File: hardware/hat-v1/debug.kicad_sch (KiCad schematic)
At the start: 45 parts, among them J5 Tag-Connect TC2050

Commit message: HAT v1 schematic: apply adversarial review (power + digital/security/DFM)
AUTO-ON above buck EN window, BENCH no longer blocks power-off, OVP moved
to 19.2 V with input damper, Tier A parts DNP for JLC, debug links
removable for production, antenna short limited, stock footprints where
available, cap ratings/DC-bias fixes, CONSOLE_TX/RX naming.

Co-Authored-By: Claude Opus 5.5 <noreply@anthropic.com>
Claude-Session: https://claude.ai/code/session_01MLRuxTEmuMV82xcNLE62jW
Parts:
- added R40, R41, R42, R43, R44, R45, R46, R47: 0R, Resistor_SMD:R_0402_1005Metric, symbol batman:R
- added R48: 1k, Resistor_SMD:R_0402_1005Metric, symbol batman:R
- J5: Note UART0 = passwordless root console until #137 ships: release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 -> console = passwordless root until #137 ships: release gate; now left out of the parts list
- TP16, TP17, TP18, TP19, TP20, TP21, TP22, TP23, TP24, TP25, TP26, TP27, TP28, TP29, TP30, TP31, TP32, TP33, TP34, TP35, TP36, TP37, TP38, TP39, TP40, TP41, TP42, TP43, TP44: now left out of the parts list
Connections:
- net 3V3_PI: now also R48.1; no longer J5.1
- net HALOW_BUSY: now also R47.1; no longer J5.10
- net HALOW_IRQ: now also R46.1; no longer J5.9
- net SPI0_CE0: now also R45.1; no longer J5.8
- net SPI0_MISO: now also R44.1; no longer J5.7
- net SPI0_MOSI: now also R43.1; no longer J5.6
- net SPI0_SCLK: now also R42.1; no longer J5.5
- net UART0_RX renamed TC_RX
- net TC_RX: now also R41.2
- net UART0_TX renamed TC_TX
- net TC_TX: now also R40.2
- new net CONSOLE_RX: R41.1
- new net CONSOLE_TX: R40.1
- new net TC_3V3: J5.1, R48.2
- new net TC_BUSY: J5.10, R47.2
- new net TC_CS: J5.8, R45.2
- new net TC_IRQ: J5.9, R46.2
- new net TC_MISO: J5.7, R44.2
- new net TC_MOSI: J5.6, R43.2
- new net TC_SCLK: J5.5, R42.2
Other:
- note added: "NOTES J5: console = passwordless root until #137 ships: release gate R48: sense only: an adapter that drives VCC cannot back-feed the Pi R40: R40-R47 debug links: fitted on dev boards, NOT fitted on production (HaLow keys cross SPI0) TP41: Kelvin pad on the shunt: mV x 100 = mA (R9) TP42: Kelvin pad on the shunt: mV x 100 = mA (R9) TP43: Kelvin pad on the shunt: mV x 100 = mA (R9) TP44: Kelvin pa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"
- note removed: "NOTES J5: UART0 = passwordless root console until #137 ships: release gate TP41: Kelvin pad on the shunt: mV x 100 = mA (R9) TP42: Kelvin pad on the shunt: mV x 100 = mA (R9) TP43: Kelvin pad on the shunt: mV x 100 = mA (R9) TP44: Kelvin pad on the shunt: mV x 100 = mA (R9)"
- moved on the sheet: J5, TP1, TP10, TP11, TP12, TP13, TP14, TP15, TP16, TP17, TP18, TP19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

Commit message: HAT v1: reduce test points (clip pads only for VBAT/5V/3V3 HaLow/GND), re-place
Signals on the 40-pin header are probed on its solder joints; checker
verifies that list. Floorplan: all functional parts and the 4 clip pads
fit; 23 small probe pads still need a home.

Co-Authored-By: Claude Opus 5.5 <noreply@anthropic.com>
Claude-Session: https://claude.ai/code/session_01MLRuxTEmuMV82xcNLE62jW
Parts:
- removed TP30: EN_5V, TestPoint:TestPoint_Pad_D1.0mm, symbol batman:TP
- removed TP31: EN_3V3, TestPoint:TestPoint_Pad_D1.0mm, symbol batman:TP
- removed TP32: PG_5V, TestPoint:TestPoint_Pad_D1.0mm, symbol batman:TP
- removed TP33: BAT_PRESENT_N, TestPoint:TestPoint_Pad_D1.0mm, symbol batman:TP
- removed TP34: EF_FLT_N, TestPoint:TestPoint_Pad_D1.0mm, symbol batman:TP
- removed TP35: EF_SHDN, TestPoint:TestPoint_Pad_D1.0mm, symbol batman:TP
- removed TP36: INA_ALERT_N, TestPoint:TestPoint_Pad_D1.0mm, symbol batman:TP
- removed TP37: RTC_CLKOUT, TestPoint:TestPoint_Pad_D1.0mm, symbol batman:TP
- removed TP38: RTC_INT_N, TestPoint:TestPoint_Pad_D1.0mm, symbol batman:TP
- removed TP39: HALOW_RESET_N, TestPoint:TestPoint_Pad_D1.0mm, symbol batman:TP
- removed TP40: HALOW_WAKE, TestPoint:TestPoint_Pad_D1.0mm, symbol batman:TP
- removed TP41: K1+ (R9), TestPoint:TestPoint_Pad_D1.0mm, symbol batman:TP
- removed TP42: K1- (R9), TestPoint:TestPoint_Pad_D1.0mm, symbol batman:TP
- removed TP43: K2+ (R22), TestPoint:TestPoint_Pad_D1.0mm, symbol batman:TP
- removed TP44: K2- (R22), TestPoint:TestPoint_Pad_D1.0mm, symbol batman:TP
- TP10: value 3V3_GNSS 3.2-3.4 -> 3V3_SEC 3.2-3.4; footprint TestPoint:TestPoint_Keystone_5015_Micro-Minature -> TestPoint:TestPoint_Pad_D1.5mm; now left out of the parts list
- TP11: value VRTC 0-3.3 -> 3V3_GNSS 3.2-3.4; footprint TestPoint:TestPoint_Keystone_5015_Micro-Minature -> TestPoint:TestPoint_Pad_D1.5mm; now left out of the parts list
- TP12: value GND -> VRTC 0-3.3; footprint TestPoint:TestPoint_Keystone_5015_Micro-Minature -> TestPoint:TestPoint_Pad_D1.5mm; now left out of the parts list
- TP13: footprint TestPoint:TestPoint_Keystone_5015_Micro-Minature -> TestPoint:TestPoint_Pad_D1.5mm; now left out of the parts list
- TP14: value GND -> GNSS_RST_N; footprint TestPoint:TestPoint_Keystone_5015_Micro-Minature -> TestPoint:TestPoint_Pad_D1.0mm; now left out of the parts list
- TP15: value GND -> GNSS_SAFEBOOT_N; footprint TestPoint:TestPoint_Keystone_5015_Micro-Minature -> TestPoint:TestPoint_Pad_D1.0mm; now left out of the parts list
- TP16: value I2C1_SDA -> PWR_BTN_N
- TP17: value I2C1_SCL -> LTC_KILL_N
- TP18: value ID_SD -> LTC_ENB
- TP19: value ID_SC -> EN_5V
- TP2: value VSYS 6-17V -> 5V 5.10-5.25
- TP20: value UART5_TX -> EN_3V3
- TP21: value UART5_RX -> PG_5V
- TP22: value GNSS_PPS -> EF_FLT_N
- TP23: value GNSS_RST_N -> EF_SHDN
- TP24: value GNSS_SAFEBOOT_N -> RTC_CLKOUT
- TP25: value PWR_BTN_N -> RTC_INT_N
- TP26: value PWR_INT_N -> K1+ (R9); Note (none) -> Kelvin pads on the shunts: R9 mV x 100 = mA, R22 mV x 50 = 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
- TP27: value LTC_KILL_N -> K1- (R9)
- TP28: value KILL_REQ -> K2+ (R22)
- TP29: value LTC_ENB -> K2- (R22)
- TP3: value 5V 5.10-5.25 -> 3V3 HaLow 3.2-3.4
- TP4: value 5V_PI 5.0-5.2 -> GND
- TP5: value OR 5-17V -> VSYS 6-17V; footprint TestPoint:TestPoint_Keystone_5015_Micro-Minature -> TestPoint:TestPoint_Pad_D1.5mm; now left out of the parts list
- TP6: value 3V3 3.25-3.40 -> 5V_PI 5.0-5.2; footprint TestPoint:TestPoint_Keystone_5015_Micro-Minature -> TestPoint:TestPoint_Pad_D1.5mm; now left out of the parts list
- TP7: value 3V3_MPCIE 3.2-3.4 -> OR 5-17V; footprint TestPoint:TestPoint_Keystone_5015_Micro-Minature -> TestPoint:TestPoint_Pad_D1.5mm; now left out of the parts list
- TP8: value 3V3_PI 3.2-3.4 -> 3V3_BUCK 3.25-3.40; footprint TestPoint:TestPoint_Keystone_5015_Micro-Minature -> TestPoint:TestPoint_Pad_D1.5mm; now left out of the parts list
- TP9: value 3V3_SEC 3.2-3.4 -> 3V3_PI 3.2-3.4; footprint TestPoint:TestPoint_Keystone_5015_Micro-Minature -> TestPoint:TestPoint_Pad_D1.5mm; now left out of the parts list
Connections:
- net GNSS_PPS is gone; now on net EF_FLT_N: TP22.1
- net I2C1_SCL is gone; now on net LTC_KILL_N: TP17.1
- net I2C1_SDA is gone; now on net PWR_BTN_N: TP16.1
- net ID_SC is gone; now on net EN_5V: TP19.1
- net ID_SD is gone; now on net LTC_ENB: TP18.1
- net KILL_REQ is gone; now on net 3V3_BUCK: TP28.1
- net PWR_INT_N is gone; now on net EF_OUT: TP26.1
- net UART5_RX is gone; now on net PG_5V: TP21.1
- net UART5_TX is gone; now on net EN_3V3: TP20.1
- net 3V3_BUCK: now also TP8.1; no longer TP6.1
- net 3V3_GNSS: now also TP11.1; no longer TP10.1
- net 3V3_MPCIE: now also TP3.1; no longer TP7.1
- net 3V3_PI: now also TP9.1; no longer TP8.1
- net 3V3_SEC: now also TP10.1; no longer TP9.1
- net 3V3_SH: now also TP29.1
- net 5V_BUCK: now also TP2.1; no longer TP3.1
- net 5V_PI: now also TP6.1; no longer TP4.1
- net EF_SHDN: now also TP23.1
- net GND: now also TP4.1; no longer TP12.1, TP14.1, TP15.1
- net GNSS_RST_N: now also TP14.1; no longer TP23.1
- net GNSS_SAFEBOOT_N: now also TP15.1; no longer TP24.1
- net LTC_ENB: no longer TP29.1
- net LTC_KILL_N: no longer TP27.1
- net OR_NODE: now also TP7.1; no longer TP5.1
- net PWR_BTN_N: no longer TP25.1
- net RTC_CLKOUT: now also TP24.1
- net RTC_INT_N: now also TP25.1
- net VRTC: now also TP12.1; no longer TP11.1
- net VSYS: now also TP27.1, TP5.1; no longer TP2.1
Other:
- note added: "NOTES J5: console = passwordless root until #137 ships: release gate R48: sense only: an adapter that drives VCC cannot back-feed the Pi R40: R40-R47 debug links: fitted on dev boards, NOT fitted on production (HaLow keys cross SPI0) TP26: Kelvin pads on the shunts: R9 mV x 100 = mA, R22 mV x 50 = mA"
- note removed: "NOTES J5: console = passwordless root until #137 ships: release gate R48: sense only: an adapter that drives VCC cannot back-feed the Pi R40: R40-R47 debug links: fitted on dev boards, NOT fitted on production (HaLow keys cross SPI0) TP41: Kelvin pad on the shunt: mV x 100 = mA (R9) TP42: Kelvin pad on the shunt: mV x 100 = mA (R9) TP43: Kelvin pad on the shunt: mV x 100 = mA (R9) TP44: Kelvin pa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"
- moved on the sheet: R45, R46, R47, TP1, TP10, TP11, TP12, TP13, TP14, TP15, TP16, TP17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

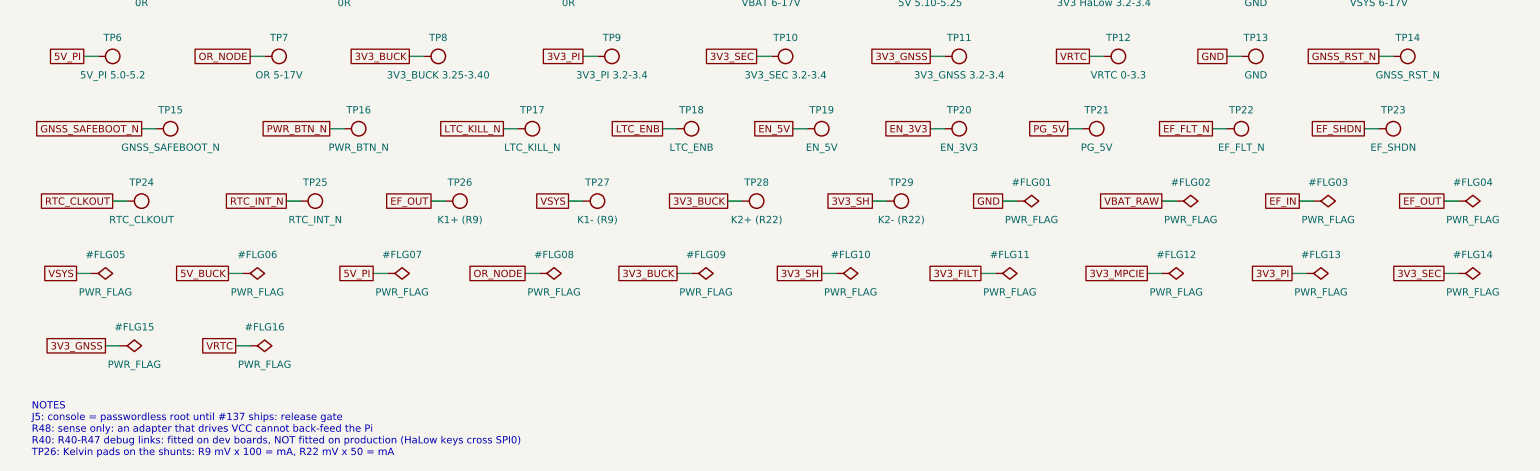
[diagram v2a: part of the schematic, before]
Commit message: HAT v1: GNSS 3-pin antenna supervisor (UBX-20053088 Fig 38) + RTC coin-cell backup
Antenna supply switched by LNA_EN, 10R sense, OPA333 comparator for open
detection, SCL/SDA reused for ANT_SHORT_N/ANT_DETECT. RTC backup moves to
a Seiko MS rechargeable cell with 1k series resistor (App Manual 7.3);
overlay trickle 15k. Cell footprint does not fit yet (floorplan).

Co-Authored-By: Claude Opus 5.5 <noreply@anthropic.com>
Claude-Session: https://claude.ai/code/session_01MLRuxTEmuMV82xcNLE62jW
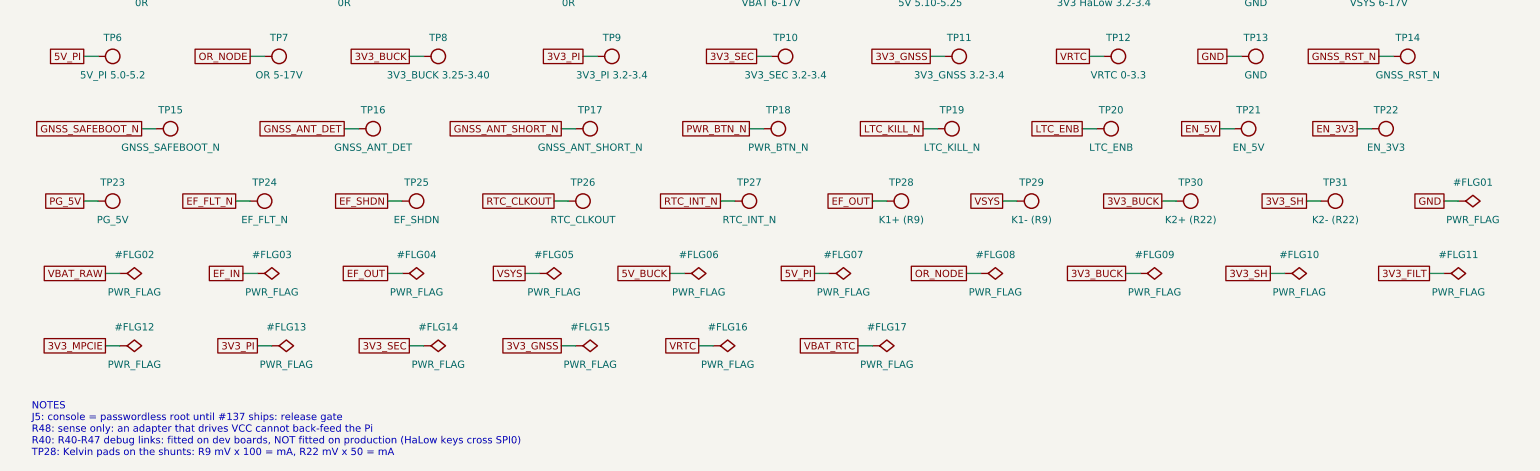
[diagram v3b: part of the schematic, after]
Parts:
- added TP30: K2+ (R22), TestPoint:TestPoint_Pad_D1.0mm, symbol batman:TP
- added TP31: K2- (R22), TestPoint:TestPoint_Pad_D1.0mm, symbol batman:TP
- TP16: value PWR_BTN_N -> GNSS_ANT_DET
- TP17: value LTC_KILL_N -> GNSS_ANT_SHORT_N
- TP18: value LTC_ENB -> PWR_BTN_N
- TP19: value EN_5V -> LTC_KILL_N
- TP20: value EN_3V3 -> LTC_ENB
- TP21: value PG_5V -> EN_5V
- TP22: value EF_FLT_N -> EN_3V3
- TP23: value EF_SHDN -> PG_5V
- TP24: value RTC_CLKOUT -> EF_FLT_N
- TP25: value RTC_INT_N -> EF_SHDN
- TP26: value K1+ (R9) -> RTC_CLKOUT; Note Kelvin pads on the shunts: R9 mV x 100 = mA, R22 mV x 50 = 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 -> (none)
- TP27: value K1- (R9) -> RTC_INT_N
- TP28: value K2+ (R22) -> K1+ (R9); Note (none) -> Kelvin pads on the shunts: R9 mV x 100 = mA, R22 mV x 50 = 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
- TP29: value K2- (R22) -> K1- (R9)
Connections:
- net 3V3_BUCK: now also TP30.1; no longer TP28.1
- net 3V3_SH: now also TP31.1; no longer TP29.1
- net EF_FLT_N: now also TP24.1; no longer TP22.1
- net EF_OUT: now also TP28.1; no longer TP26.1
- net EF_SHDN: now also TP25.1; no longer TP23.1
- net EN_3V3: now also TP22.1; no longer TP20.1
- net EN_5V: now also TP21.1; no longer TP19.1
- net LTC_ENB: now also TP20.1; no longer TP18.1
- net LTC_KILL_N: now also TP19.1; no longer TP17.1
- net PG_5V: now also TP23.1; no longer TP21.1
- net PWR_BTN_N: now also TP18.1; no longer TP16.1
- net RTC_CLKOUT: now also TP26.1; no longer TP24.1
- net RTC_INT_N: now also TP27.1; no longer TP25.1
- net VSYS: now also TP29.1; no longer TP27.1
- new net GNSS_ANT_DET: TP16.1
- new net GNSS_ANT_SHORT_N: TP17.1
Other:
- note added: "NOTES J5: console = passwordless root until #137 ships: release gate R48: sense only: an adapter that drives VCC cannot back-feed the Pi R40: R40-R47 debug links: fitted on dev boards, NOT fitted on production (HaLow keys cross SPI0) TP28: Kelvin pads on the shunts: R9 mV x 100 = mA, R22 mV x 50 = mA"
- note removed: "NOTES J5: console = passwordless root until #137 ships: release gate R48: sense only: an adapter that drives VCC cannot back-feed the Pi R40: R40-R47 debug links: fitted on dev boards, NOT fitted on production (HaLow keys cross SPI0) TP26: Kelvin pads on the shunts: R9 mV x 100 = mA, R22 mV x 50 = mA"
- moved on the sheet: TP16, TP17, TP18, TP19, TP20, TP21, TP22, TP23, TP24, TP25, TP26, TP27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

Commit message: HAT v1: keep the CPH3225A supercap for RTC backup (user decision)
Co-Authored-By: Claude Opus 5.5 <noreply@anthropic.com>
Claude-Session: https://claude.ai/code/session_01MLRuxTEmuMV82xcNLE62jW
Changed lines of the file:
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@@
   (global_label "VRTC" (shape passive) (at 132.08 115.57 180) (fields_autoplaced) (effects (font (size 1.27 1.27)) (justify right))
     (property "Intersheetrefs" "${INTERSHEET_REFS}" (at 132.08 115.57 0) (effects (font (size 1.27 1.27)) hide)))
-  (symbol (lib_id "batman:PWR_FLAG") (at 165.1 115.57 0) (unit 1) (in_bom no) (on_board no) (dnp no)
-    (property "Reference" "#FLG17" (at 165.1 113.03 0) (effects (font (size 1.27 1.27)) (justify bottom)))
-    (property "Value" "PWR_FLAG" (at 165.1 118.11 0) (effects (font (size 1.27 1.27)) (justify top)))
-    (property "Footprint" "" (at 165.1 115.57 0) (effects (font (size 1.27 1.27)) hide))
-    (property "Datasheet" "" (at 165.1 115.57 0) (effects (font (size 1.27 1.27)) hide))
-    (property "MPN" "" (at 165.1 115.57 0) (effects (font (size 1.27 1.27)) hide))
-    (property "Manufacturer" "" (at 165.1 115.57 0) (effects (font (size 1.27 1.27)) hide))
-    (property "Tier" "C" (at 165.1 115.57 0) (effects (font (size 1.27 1.27)) hide))
-    (property "LCSC" "" (at 165.1 115.57 0) (effects (font (size 1.27 1.27)) hide))
-    (property "Note" "" (at 165.1 115.57 0) (effects (font (size 1.27 1.27)) hide))
-    (pin "1")
-    (instances (project "batman-hat" (path "/bad0bf22-4662-5834-886f-55d01014b15a/02b90d21-87d4-50f6-94db-12e47b95b656" (reference "#FLG17") (unit 1))))
-  )
-  (wire (pts (xy 162.56 115.57) (xy 160.02 115.57)) (stroke (width 0) (type default)))
-  (global_label "VBAT_RTC" (shape passive) (at 160.02 115.57 180) (fields_autoplaced) (effects (font (size 1.27 1.27)) (justify right))
-    (property "Intersheetrefs" "${INTERSHEET_REFS}" (at 160.02 115.57 0) (effects (font (size 1.27 1.27)) hide)))
   (text "NOTES\nJ5: console = passwordless root until #137 ships: release gate\nR48: sense only: an adapter that drives VCC cannot back-feed the Pi\nR40: R40-R47 debug links: fitted on dev boards, NOT fitted on production (HaLow keys cross SPI0)\nTP28: Kelvin pads on the shunts: R9 mV x 100 = mA, R22 mV x 50 = mA" (at 15 125.48 0) (effects (font (size 1.27 1.27)) (justify left top)))
 )
